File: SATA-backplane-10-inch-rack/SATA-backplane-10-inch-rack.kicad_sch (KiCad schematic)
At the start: 23 parts, among them J101 Conn_01x06, Q101 DMG1012UW, Q102 DMG1012UW

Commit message: Fiddling with layout
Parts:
- removed H1, H2, H3, H4, H5, H6: MountingHole, MountingHole:MountingHole_3.7mm, symbol Mechanical:MountingHole
- added JP102: SolderJumper, Jumper:SolderJumper-2_P1.3mm_Open_RoundedPad1.0x1.5mm, symbol Jumper:SolderJumper_2_Open
- added U1: NCP1117-3.3_SOT223, Package_TO_SOT_SMD:SOT-223-3_TabPin2, symbol Regulator_Linear:NCP1117-3.3_SOT223
- D104: footprint LED_SMD:LED_0805_2012Metric_Pad1.15x1.40mm_HandSolder -> LED_SMD:LED_1206_3216Metric_Pad1.42x1.75mm_HandSolder
- Q101, Q102: footprint Package_TO_SOT_SMD:SOT-323_SC-70 -> Package_TO_SOT_SMD:SOT-323_SC-70_Handsoldering; I_{dss} 5nA -> (none); I_{d} 640mA -> (none); I_{gss} ±1µA -> (none); Mouser No 621-DMG1012UW-7 -> (none); Mouser Part Number (none) -> 621-DMG1012UW-7; V_{gs} ±6V -> (none)
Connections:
- net +3.3V: now also JP102.2 (B)
- net +5V: now also U1.3 (VI)
- net GND: now also U1.1 (GND)
- new net: JP102.1 (A), U1.2 (VO)
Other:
- moved on the sheet: C104, D104, JP101, Q101, Q102, R101, R102, R103, R104, R105

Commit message: Place & Route
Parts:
- added MECH1: 3D print, symbol Mechanical:Heatsink
- JP101, JP102: value SolderJumper -> Jumper; footprint Jumper:SolderJumper-2_P1.3mm_Open_RoundedPad1.0x1.5mm -> Connector_PinHeader_2.54mm:PinHeader_1x02_P2.54mm_Horizontal; symbol Jumper:SolderJumper_2_Open -> Jumper:Jumper_2_Small_Open; now in the parts list
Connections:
- net +12V: now also J101.6 (Pin_6); no longer J101.5 (Pin_5)
- net +3.3V: now also J101.2 (Pin_2), JP102.1 (A); no longer J101.1 (Pin_1), JP102.2 (B)
- net +5V: now also J101.4 (Pin_4); no longer J101.3 (Pin_3)
- net GND: now also J101.1 (Pin_1), J101.3 (Pin_3), J101.5 (Pin_5); no longer J101.2 (Pin_2), J101.4 (Pin_4), J101.6 (Pin_6)
- net STA_N: now also JP101.1 (A); no longer JP101.2 (B)
- net at C104.2, R101.1: now also JP101.2 (B); no longer JP101.1 (A)
- net at U1.2 (VO): now also JP102.2 (B); no longer JP102.1 (A)
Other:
- moved on the sheet: J101
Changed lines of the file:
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@@
 	(wire
 		(pts
-			(xy 66.04 99.06) (xy 68.58 99.06)
+			(xy 227.33 78.74) (xy 238.76 78.74)
 		)
 		(stroke
@@
 	(wire
 		(pts
-			(xy 220.98 38.1) (xy 233.68 38.1)
-		)
-		(stroke
-			(width 0)
-			(type default)
-		)
-	)
-	(wire
-		(pts
-			(xy 128.27 90.17) (xy 128.27 93.98)
+			(xy 66.04 99.06) (xy 68.58 99.06)
 		)
 		(stroke
@@
 	(wire
 		(pts
-			(xy 233.68 48.26) (xy 233.68 50.8)
+			(xy 220.98 38.1) (xy 233.68 38.1)
 		)
 		(stroke
@@
 	(wire
 		(pts
-			(xy 182.88 48.26) (xy 182.88 50.8)
+			(xy 128.27 90.17) (xy 128.27 93.98)
 		)
 		(stroke
@@
 	(wire
 		(pts
-			(xy 83.82 99.06) (xy 81.28 99.06)
+			(xy 233.68 48.26) (xy 233.68 50.8)
 		)
 		(stroke
@@
 	(wire
 		(pts
-			(xy 228.6 78.74) (xy 238.76 78.74)
+			(xy 182.88 48.26) (xy 182.88 50.8)
 		)
 		(stroke
@@
 	(wire
 		(pts
-			(xy 68.58 99.06) (xy 73.66 99.06)
+			(xy 68.58 99.06) (xy 74.93 99.06)
 		)
 		(stroke
@@
 	(wire
 		(pts
-			(xy 86.36 35.56) (xy 91.44 35.56)
+			(xy 86.36 50.8) (xy 91.44 50.8)
 		)
 		(stroke
@@
 	(wire
 		(pts
+			(xy 80.01 99.06) (xy 83.82 99.06)
+		)
+		(stroke
+			(width 0)
+			(type default)
+		)
+	)
+	(wire
+		(pts
 			(xy 86.36 38.1) (xy 91.44 38.1)
 		)
@@
 	(wire
 		(pts
-			(xy 209.55 78.74) (xy 220.98 78.74)
+			(xy 209.55 78.74) (xy 222.25 78.74)
 		)
 		(stroke
@@
 	)
 	(label "GND"
-		(at 91.44 35.56 180)
+		(at 91.44 50.8 180)
 		(effects
 			(font
@@
 	)
 	(symbol
-		(lib_id "Jumper:SolderJumper_2_Open")
+		(lib_id "Jumper:Jumper_2_Small_Open")
 		(at 77.47 99.06 0)
+		(mirror y)
 		(unit 1)
 		(exclude_from_sim no)
-		(in_bom no)
+		(in_bom yes)
 		(on_board yes)
 		(dnp no)
-		(fields_autoplaced yes)
 		(property "Reference" "JP101"
 			(at 77.47 92.71 0)
@@
 			)
 		)
-		(property "Value" "SolderJumper"
+		(property "Value" "Jumper"
 			(at 77.47 95.25 0)
 			(effects
@@
 			)
 		)
-		(property "Footprint" "Jumper:SolderJumper-2_P1.3mm_Open_RoundedPad1.0x1.5mm"
+		(property "Footprint" "Connector_PinHeader_2.54mm:PinHeader_1x02_P2.54mm_Horizontal"
 			(at 77.47 99.06 0)
 			(effects
@@
 			)
 		)
-		(property "Description" "Solder Jumper, 2-pole, open"
+		(property "Description" "Jumper, 2-pole, small symbol, open"
 			(at 77.47 99.06 0)
 			(effects
@@
 	)
 	(symbol
+		(lib_id "Mechanical:Heatsink")
+		(at 26.67 176.53 0)
+		(unit 1)
+		(exclude_from_sim no)
+		(in_bom no)
+		(on_board yes)
+		(dnp no)
+		(fields_autoplaced yes)
+		(property "Reference" "MECH1"
+			(at 30.48 173.3549 0)
+			(effects
+				(font
+					(size 1.27 1.27)
+				)
+				(justify left)
+			)
+		)
+		(property "Value" "3D print"
+			(at 30.48 175.8949 0)
+			(effects
+				(font
+					(size 1.27 1.27)
+				)
+				(justify left)
+			)
+		)
+		(property "Footprint" ""
+			(at 26.9748 176.53 0)
+			(effects
+				(font
+					(size 1.27 1.27)
+				)
+				(hide yes)
+			)
+		)
+		(property "Datasheet" "~"
+			(at 26.9748 176.53 0)
+			(effects
+				(font
+					(size 1.27 1.27)
+				)
+				(hide yes)
+			)
+		)
+		(property "Description" "Heatsink"
+			(at 26.67 176.53 0)
+			(effects
+				(font
+					(size 1.27 1.27)
+				)
+				(hide yes)
+			)
+		)
+		(instances
+			(project ""
+				(path "/c1a10ee3-1b0d-4235-ba02-c6ac86e8d48c"
+					(reference "MECH1")
+					(unit 1)
+				)
+			)
+		)
+	)
+	(symbol
 		(lib_id "power:+5V")
 		(at 182.88 38.1 0)
@@
 	(symbol
 		(lib_id "Connector_Generic:Conn_01x06")
-		(at 81.28 43.18 180)
+		(at 81.28 45.72 180)
 		(unit 1)
 		(exclude_from_sim no)
@@
 		(dnp no)
 		(property "Reference" "J101"
-			(at 78.74 43.1801 0)
+			(at 78.74 45.7201 0)
 			(effects
 				(font
@@
 		)
 		(property "Value" "Conn_01x06"
-			(at 78.74 40.6401 0)
+			(at 78.74 43.1801 0)
 			(effects
 				(font
@@
 		)
 		(property "Footprint" "TerminalBlock_Phoenix_PT-1,5-6-3.5-H_1x06_P3.50mm_Horizontal"
-			(at 81.28 43.18 0)
+			(at 81.28 45.72 0)
 			(effects
 				(font
@@
 		)
 		(property "Datasheet" "~"
-			(at 81.28 43.18 0)
+			(at 81.28 45.72 0)
 			(effects
 				(font
@@
 		)
 		(property "Description" "Generic connector, single row, 01x06, script generated (kicad-library-utils/schlib/autogen/connector/)"
-			(at 81.28 43.18 0)
+			(at 81.28 45.72 0)
 			(effects
 				(font
@@
 		)
 		(property "Mouser Part Number" "651-1984659"
-			(at 81.28 43.18 0)
+			(at 81.28 45.72 0)
 			(effects
 				(font
@@
 		)
 		(property "Manufacturer_Part_Number" "1984659"
-			(at 81.28 43.18 0)
+			(at 81.28 45.72 0)
 			(effects
 				(font
@@
 		)
 		(property "Manufacturer_Name" "Phoenix Contact"
-			(at 81.28 43.18 0)
+			(at 81.28 45.72 0)
 			(effects
 				(font
@@
 	)
 	(symbol
-		(lib_id "Jumper:SolderJumper_2_Open")
+		(lib_id "Jumper:Jumper_2_Small_Open")
 		(at 224.79 78.74 0)
+		(mirror y)
 		(unit 1)
 		(exclude_from_sim no)
-		(in_bom no)
+		(in_bom yes)
 		(on_board yes)
 		(dnp no)
-		(fields_autoplaced yes)
 		(property "Reference" "JP102"
 			(at 224.79 72.39 0)
@@
 			)
 		)
-		(property "Value" "SolderJumper"
+		(property "Value" "Jumper"
 			(at 224.79 74.93 0)
 			(effects
@@
 			)
 		)
-		(property "Footprint" "Jumper:SolderJumper-2_P1.3mm_Open_RoundedPad1.0x1.5mm"
+		(property "Footprint" "Connector_PinHeader_2.54mm:PinHeader_1x02_P2.54mm_Horizontal"
 			(at 224.79 78.74 0)
 			(effects
@@
 			)
 		)
-		(property "Description" "Solder Jumper, 2-pole, open"
+		(property "Description" "Jumper, 2-pole, small symbol, open"
 			(at 224.79 78.74 0)
 			(effects

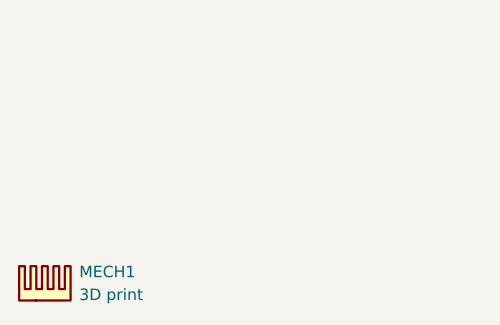
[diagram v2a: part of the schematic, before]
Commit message: Finish layout
Plus backport 3D into KiCAD
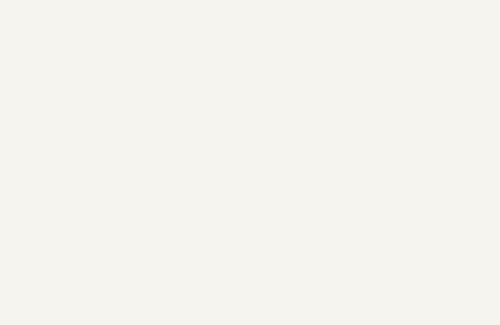
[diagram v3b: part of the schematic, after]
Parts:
- removed MECH1: 3D print, symbol Mechanical:Heatsink
- D104: footprint LED_SMD:LED_1206_3216Metric_Pad1.42x1.75mm_HandSolder -> LED_THT:LED_D3.0mm_Clear
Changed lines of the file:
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@@
 			)
 		)
-		(property "Footprint" "LED_SMD:LED_1206_3216Metric_Pad1.42x1.75mm_HandSolder"
+		(property "Footprint" "LED_THT:LED_D3.0mm_Clear"
 			(at 151.13 82.55 0)
 			(effects
@@
 					(unit 1)
 				)
-			)
-		)
-	)
-	(symbol
-		(lib_id "Mechanical:Heatsink")
-		(at 26.67 176.53 0)
-		(unit 1)
-		(exclude_from_sim no)
-		(in_bom no)
-		(on_board yes)
-		(dnp no)
-		(fields_autoplaced yes)
-		(property "Reference" "MECH1"
-			(at 30.48 173.3549 0)
-			(effects
-				(font
-					(size 1.27 1.27)
-				)
-				(justify left)
-			)
-		)
-		(property "Value" "3D print"
-			(at 30.48 175.8949 0)
-			(effects
-				(font
-					(size 1.27 1.27)
-				)
-				(justify left)
-			)
-		)
-		(property "Footprint" ""
-			(at 26.9748 176.53 0)
-			(effects
-				(font
-					(size 1.27 1.27)
-				)
-				(hide yes)
-			)
-		)
-		(property "Datasheet" "~"
-			(at 26.9748 176.53 0)
-			(effects
-				(font
-					(size 1.27 1.27)
-				)
-				(hide yes)
-			)
-		)
-		(property "Description" "Heatsink"
-			(at 26.67 176.53 0)
-			(effects
-				(font
-					(size 1.27 1.27)
-				)
-				(hide yes)
-			)
-		)
-		(instances
-			(project ""
-				(path "/c1a10ee3-1b0d-4235-ba02-c6ac86e8d48c"
-					(reference "MECH1")
-					(unit 1)
-				)

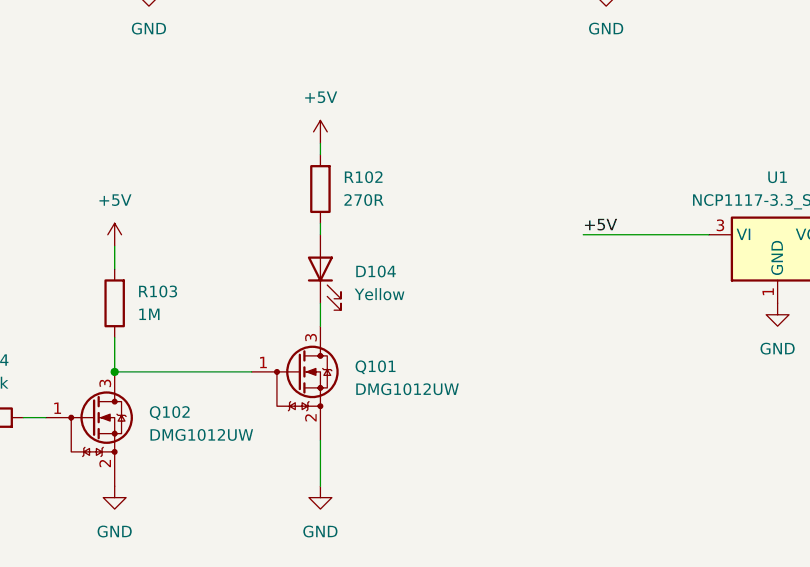
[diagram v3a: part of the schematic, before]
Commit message: Add text ACT to D104
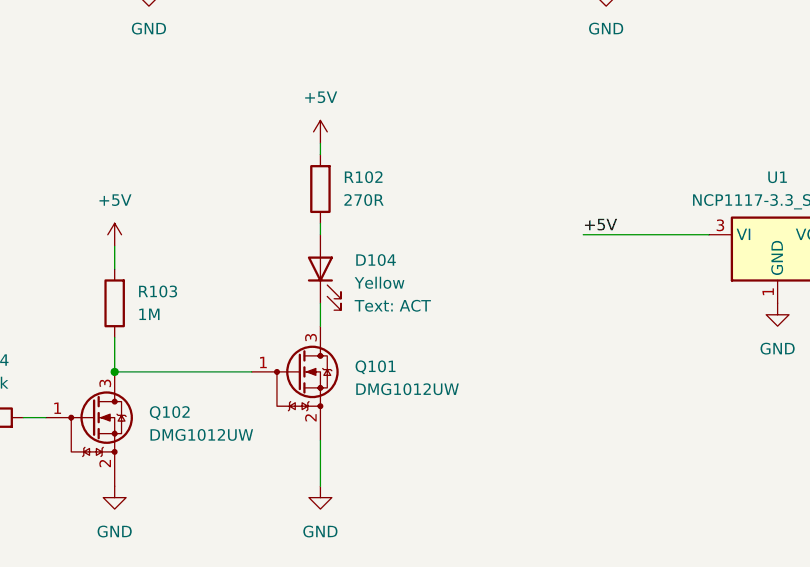
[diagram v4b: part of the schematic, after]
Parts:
- D104: Text (none) -> ACT
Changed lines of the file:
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@@
 		(fields_autoplaced yes)
 		(property "Reference" "D104"
-			(at 154.94 82.8674 90)
+			(at 154.94 81.5974 90)
 			(effects
 				(font
@@
 		)
 		(property "Value" "Yellow"
-			(at 154.94 85.4074 90)
+			(at 154.94 84.1374 90)
 			(effects
 				(font
@@
 			)
 		)
+		(property "Text" "ACT"
+			(at 154.94 86.6774 90)
+			(show_name yes)
+			(effects
+				(font
+					(size 1.27 1.27)
+				)
+				(justify right)
+			)
+		)

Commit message: Schematic : define temporary mfg.partnumbers
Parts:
- C104: Manufacturer_Part_Number (none) -> 100uF 6.3V
- D104: Manufacturer_Part_Number (none) -> Yellow led
- JP101, JP102: Manufacturer_Part_Number (none) -> PinHeader_1x02_P2.54mm_bended
- R101, R103: Manufacturer_Part_Number (none) -> 1M
- R102: Manufacturer_Part_Number (none) -> 270R
- R104, R105: Manufacturer_Part_Number (none) -> 100k
- U1: Manufacturer_Part_Number (none) -> NCP1117-3.3_SOT223
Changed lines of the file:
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@@
+			)
+		)
+		(property "Manufacturer_Part_Number" "270R"
+			(at 151.13 73.66 0)
+			(effects
+				(font
+					(size 1.27 1.27)
+				)
+				(hide yes)
 			)
 		)
@@
 		)
 		(property "Description" "Resistor"
+			(at 128.27 86.36 0)
+			(effects
+				(font
+					(size 1.27 1.27)
+				)
+				(hide yes)
+			)
+		)
+		(property "Manufacturer_Part_Number" "1M"
 			(at 128.27 86.36 0)
 			(effects
@@
 			)
 		)
+		(property "Manufacturer_Part_Number" "Yellow led"
+			(at 151.13 82.55 90)
+			(effects
+				(font
+					(size 1.27 1.27)
+				)
+				(hide yes)
+			)
+		)
 		(pin "1"
 		)
@@
 		(property "Description" "Unpolarized capacitor, small symbol"
 			(at 62.23 111.76 0)
+			(effects
+				(font
+					(size 1.27 1.27)
+				)
+				(hide yes)
+			)
+		)
+		(property "Manufacturer_Part_Number" "100uF 6.3V"
+			(at 62.23 111.76 90)
 			(effects
 				(font
@@
 			)
 		)
+		(property "Manufacturer_Part_Number" "PinHeader_1x02_P2.54mm_bended"
+			(at 77.47 99.06 0)
+			(effects
+				(font
+					(size 1.27 1.27)
+				)
+				(hide yes)
+			)
+		)
 		(pin "2"
 		)
@@
 			)
 		)
+		(property "Manufacturer_Part_Number" "NCP1117-3.3_SOT223"
+			(at 201.93 78.74 0)
+			(effects
+				(font
+					(size 1.27 1.27)
+				)
+				(hide yes)
+			)
+		)
 		(pin "3"
 		)
@@
 		(property "Description" "Resistor"
 			(at 62.23 99.06 0)
+			(effects
+				(font
+					(size 1.27 1.27)
+				)
+				(hide yes)
+			)
+		)
+		(property "Manufacturer_Part_Number" "1M"
+			(at 62.23 99.06 90)
 			(effects
 				(font
@@
 			)
 		)
+		(property "Manufacturer_Part_Number" "100k"
+			(at 106.68 91.44 0)
+			(effects
+				(font
+					(size 1.27 1.27)
+				)
+				(hide yes)
+			)
+		)
 		(pin "1"
 		)
@@
 			)
 		)
+		(property "Manufacturer_Part_Number" "100k"
+			(at 114.3 99.06 90)
+			(effects
+				(font
+					(size 1.27 1.27)
+				)
+				(hide yes)
+			)
+		)
 		(pin "1"
 		)
@@
 			(at 224.79 78.74 0)
 			(effects
+				(font
+					(size 1.27 1.27)
+				)
+				(hide yes)
+			)
+		)
+		(property "Manufacturer_Part_Number" "PinHeader_1x02_P2.54mm_bended"
+			(at 224.79 78.74 0)
+			(effects
